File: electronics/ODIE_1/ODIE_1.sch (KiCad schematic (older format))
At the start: 3 parts

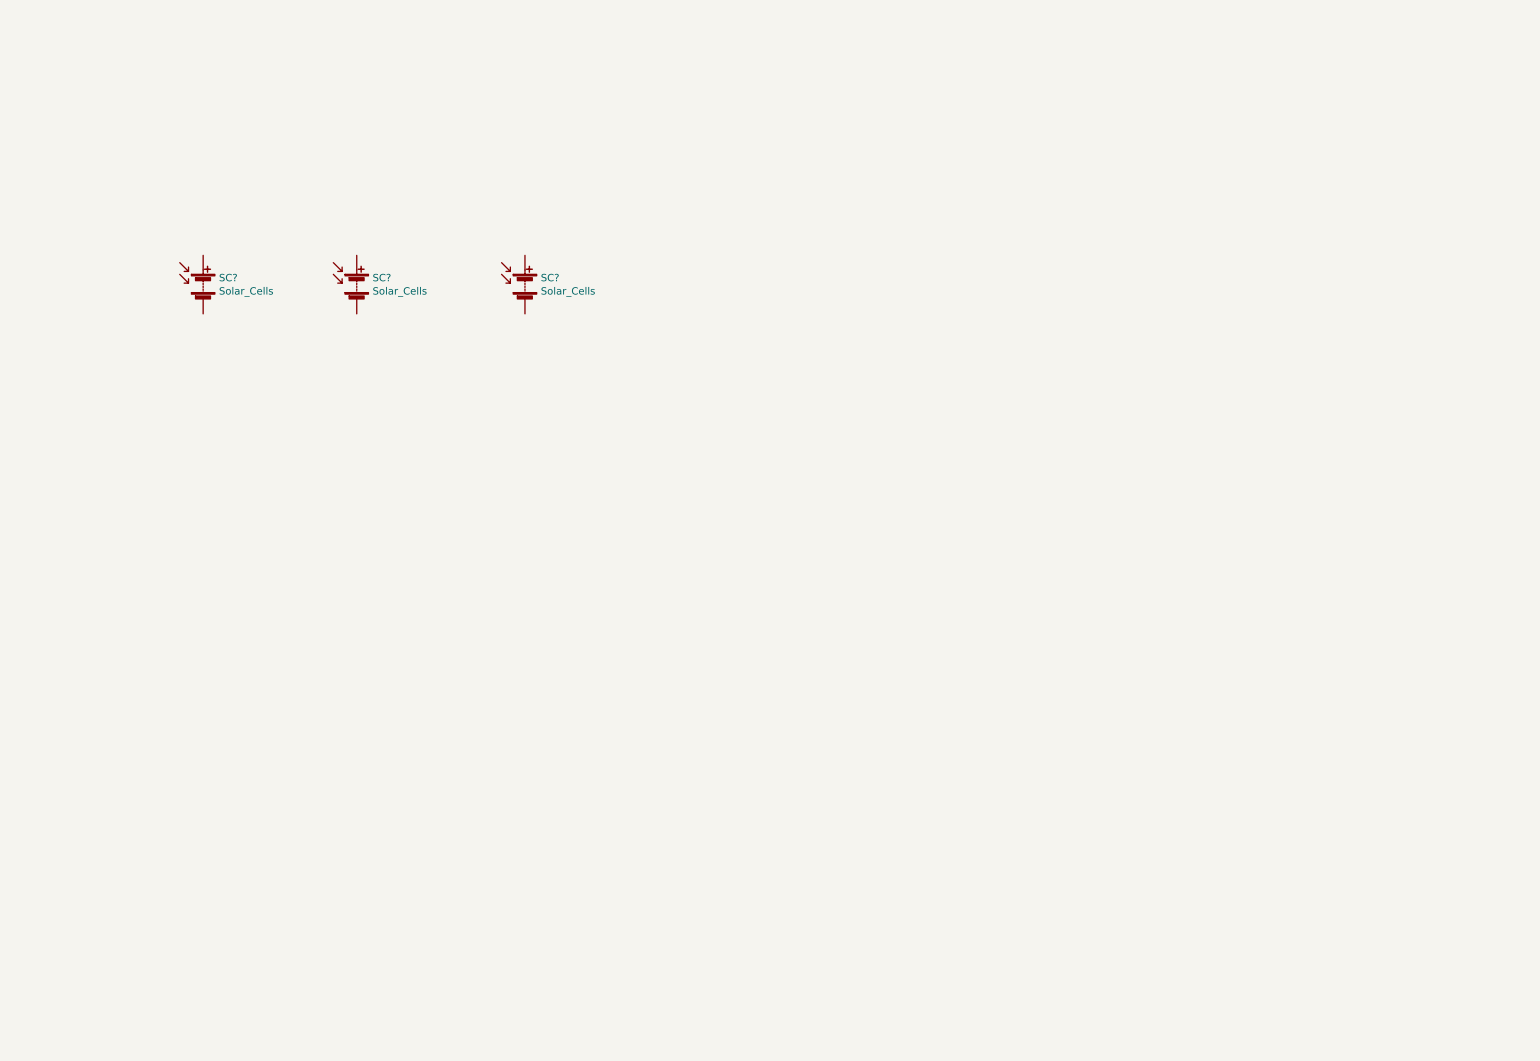
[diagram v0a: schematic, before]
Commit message: Added some sensors
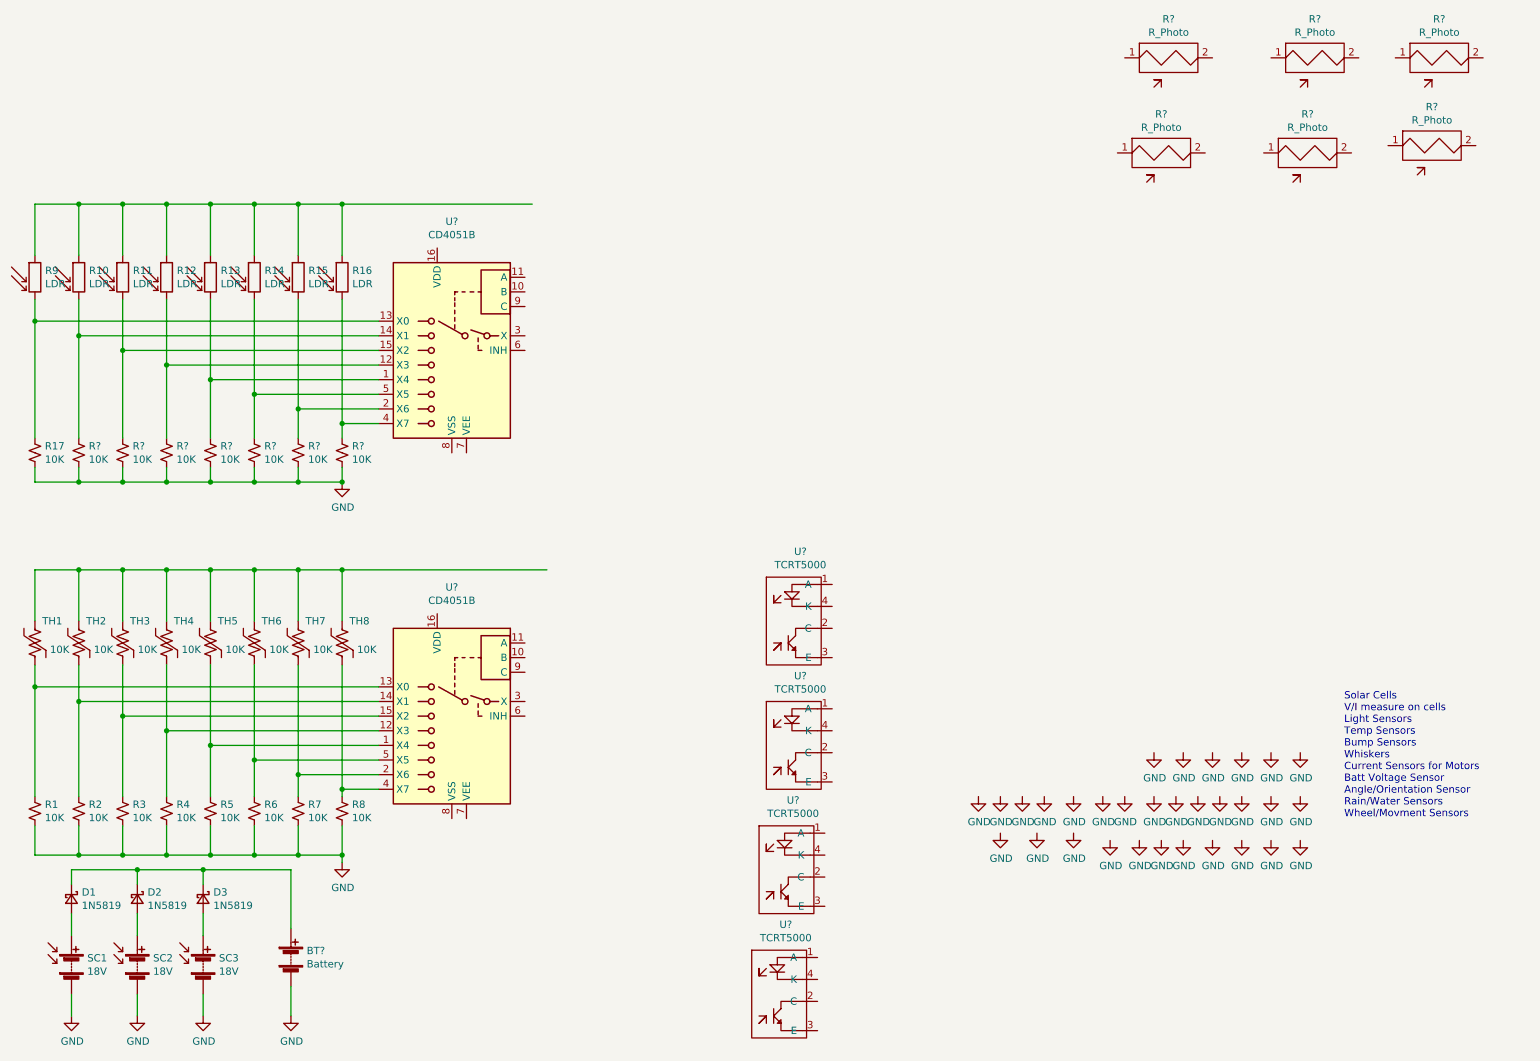
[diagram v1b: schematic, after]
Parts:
- added BT?: Battery, symbol Device:Battery
- added D1, D2, D3: 1N5819, symbol Device:D_Schottky_Small
- added R1, R17, R2, R3, R4, R5, R6, R7, R8, R? (x7): 10K, symbol Device:R_Small_US
- added R10, R11, R12, R13, R14, R15, R16, R9: LDR, symbol Device:R_PHOTO
- added R? (x6): R_Photo, symbol BDK_Passive:R_Photo
- added TH1, TH2, TH3, TH4, TH5, TH6, TH7, TH8: 10K, symbol Device:Thermistor_US
- added U? (x4): TCRT5000, symbol bdk_sensor:TCRT5000
- added U? (x2): CD4051B, symbol Analog_Switch:CD4051B
- SC1, SC2, SC3: renamed from SC?; value Solar_Cells -> 18V
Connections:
- net at SC1.1 (+): now also D1.2 (A)
- net GND: now reaches SC1.2 (-)
- net GND: now also SC2.2 (-), SC3.2 (-), BT?.2 (-), R1.2, R17.2, R2.2, R3.2, R4.2, R5.2, R6.2, R7.2, R8.2, R?.2, R?.2, R?.2, R?.2, R?.2, R?.2, R?.2
- net at SC2.1 (+): now also D2.2 (A)
- net at SC3.1 (+): now also D3.2 (A)
- new net: BT?.1 (+), D1.1 (K), D2.1 (K), D3.1 (K)
- new net: TH1.1, TH2.1, TH3.1, TH4.1, TH5.1, TH6.1, TH7.1, TH8.1
- new net: R1.1, TH1.2, U?.13 (X0)
- new net: R2.1, TH2.2, U?.14 (X1)
- new net: R3.1, TH3.2, U?.15 (X2)
- new net: R4.1, TH4.2, U?.12 (X3)
- new net: R5.1, TH5.2, U?.1 (X4)
- new net: R6.1, TH6.2, U?.5 (X5)
- new net: R7.1, TH7.2, U?.2 (X6)
- new net: R8.1, TH8.2, U?.4 (X7)
- new net: R13.2, R?.1, U?.1 (X4)
- new net: R12.2, R?.1, U?.12 (X3)
- new net: R17.1, R9.2, U?.13 (X0)
- new net: R10.2, R?.1, U?.14 (X1)
- new net: R11.2, R?.1, U?.15 (X2)
- new net: R15.2, R?.1, U?.2 (X6)
- new net: R16.2, R?.1, U?.4 (X7)
- new net: R14.2, R?.1, U?.5 (X5)
- new net: R10.1, R11.1, R12.1, R13.1, R14.1, R15.1, R16.1, R9.1
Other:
- note added: "Solar Cells\nV/I measure on cells\nLight Sensors\nTemp Sensors\nBump Sensors\nWhiskers\nCurrent Sensors for Motors\nBatt Voltage Sensor\nAngle/Orientation Sensor\nRain/Water Sensors\nWheel/Movment Sensors\n"
- moved on the sheet: SC1, SC2, SC3
